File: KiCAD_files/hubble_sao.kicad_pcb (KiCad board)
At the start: 2 copper layers, 38 x 45.5 mm, 43 parts, among them J1 Conn_02x03_Counter_Clockwise, J2 Conn_02x03_Odd_Even, Q1 DMP3099L-7, SW1 SW_Push_Shielded, SW2 SW_Push, U1 VEML3328, U2 LSM6DSO, U3 ATmega328PB-A, U4 TLV9062xD, U5 TLV9062xD

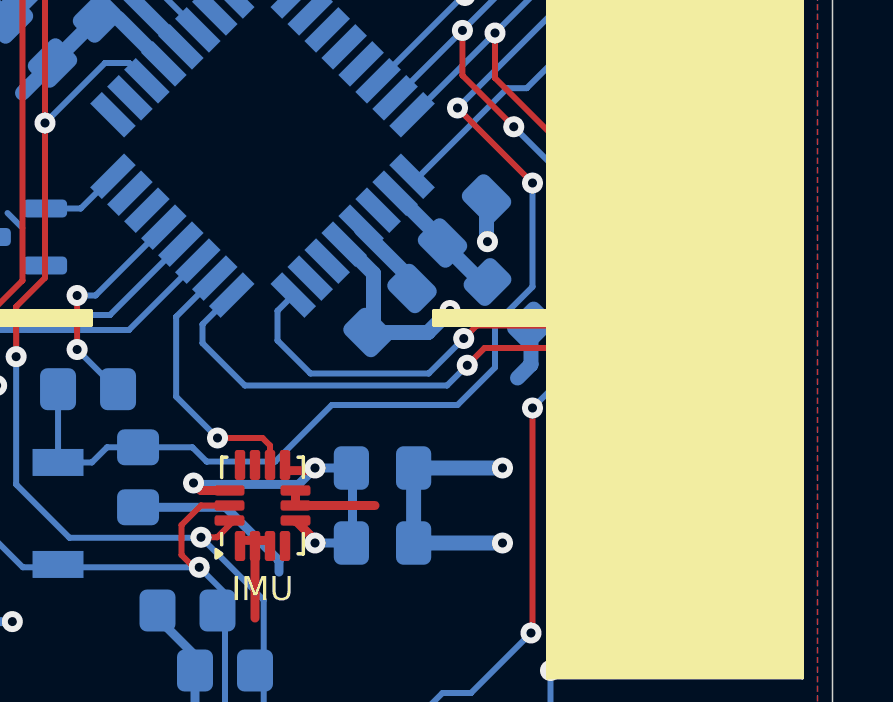
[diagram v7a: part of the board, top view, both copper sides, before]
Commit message: Moved Panel3 to 19/PE2/ADC6/ICP3
This should enable the use of the Input Capture Pin 3.
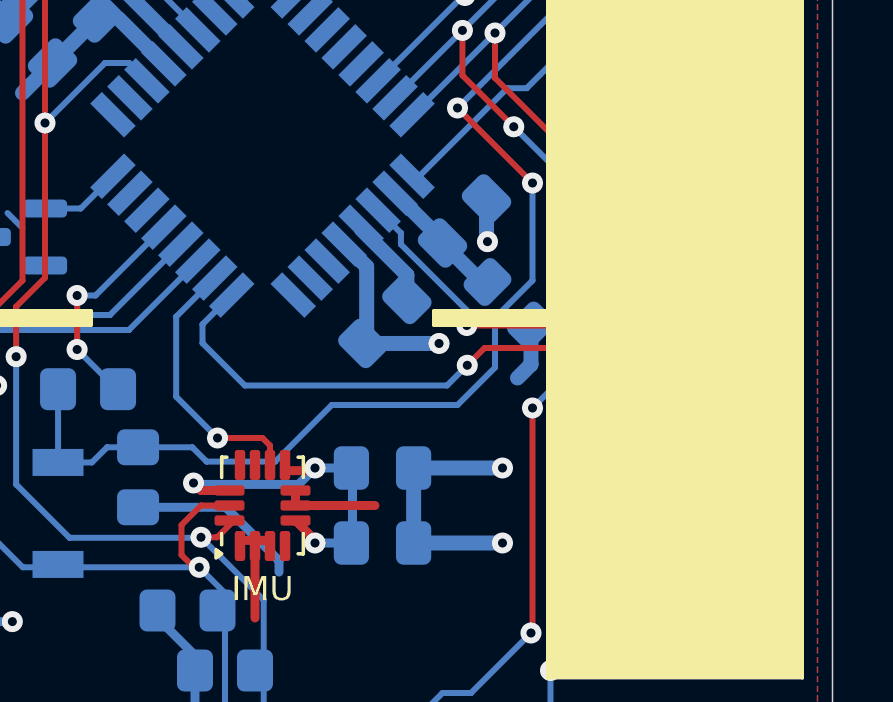
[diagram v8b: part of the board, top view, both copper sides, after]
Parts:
- moved C7 0.40 mm to (94.1, 124.6)
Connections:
- U3 pad 19: unconnected-(U3-PE2-Pad19) -> /PANEL3
- U3 pad 24: /PANEL3 -> unconnected-(U3-PC1-Pad24)
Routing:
- net /PANEL3: track 21.9 -> 17.8 mm
- net GND: track 65.9 -> 65.2 mm
- net Net-(U3-AREF): track 2.40 -> 2.98 mm
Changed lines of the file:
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@@
 	(net 10 "unconnected-(U3-XTAL1{slash}PB6-Pad7)")
 	(net 11 "unconnected-(U3-PD0-Pad30)")
-	(net 12 "unconnected-(U3-PE2-Pad19)")
+	(net 12 "unconnected-(U3-PC1-Pad24)")
 	(net 13 "unconnected-(U3-PD1-Pad31)")
 	(net 14 "/LED")
@@
 			(size 1.6 0.55)
 			(layers "B.Cu" "B.Paste" "B.Mask")
-			(net 12 "unconnected-(U3-PE2-Pad19)")
+			(net 28 "/PANEL3")
 			(pinfunction "PE2")
-			(pintype "bidirectional+no_connect")
+			(pintype "bidirectional")
 		)
 		(pad "20" smd rect
@@
 			(size 1.6 0.55)
 			(layers "B.Cu" "B.Paste" "B.Mask")
-			(net 28 "/PANEL3")
+			(net 12 "unconnected-(U3-PC1-Pad24)")
 			(pinfunction "PC1")
-			(pintype "bidirectional")
+			(pintype "bidirectional+no_connect")
 		)
 		(pad "25" smd rect
@@
 	(footprint "Capacitor_SMD:C_0805_2012Metric_Pad1.18x1.45mm_HandSolder"
 		(layer "B.Cu")
-		(at 94.25 124.25 45)
+		(at 94.078623 124.615377 45)
 		(descr "Capacitor SMD 0805 (2012 Metric), square (rectangular) end terminal, IPC_7351 nominal with elongated pad for handsoldering. (Body size source: IPC-SM-782 page 76, https://www.pcb-3d.com/wordpress/wp-content/uploads/ipc-sm-782a_amendment_1_and_2.pdf, https://docs.google.com/spreadsheets/d/1BsfQQcO9C6DZCsRaXUlFlo91Tg2WpOkGARC1WS5S8t0/edit?usp=sharing), generated with kicad-footprint-generator")
 		(tags "capacitor handsolder")
@@
 	)
 	(segment
+		(start 94.812246 123.062246)
+		(end 94.812246 123.881754)
+		(width 0.5)
+		(layer "B.Cu")
+		(net 7)
+	)
+	(segment
 		(start 93.288047 121.538047)
-		(end 94.983623 123.233623)
+		(end 94.812246 123.062246)
 		(width 0.5)
 		(layer "B.Cu")
@@
 	)
 	(via
-		(at 96.25 124.25)
+		(at 95.885 125.349)
 		(size 0.7)
 		(drill 0.3)
@@
 	)
 	(via
-		(at 100.25 130.25)
+		(at 100.457 130.175)
 		(size 0.7)
 		(drill 0.3)
@@
 	)
 	(segment
+		(start 101.4195 131.1375)
+		(end 101.5 131.1375)
+		(width 0.3)
+		(layer "B.Cu")
+		(net 20)
+	)
+	(segment
 		(start 73.5 127.11)
 		(end 74.62 127.11)
@@
 	)
 	(segment
-		(start 79.883 132.487)
-		(end 79.883 133.604)
-		(width 0.3)
+		(start 93.472 122.787686)
+		(end 92.722361 122.038047)
+		(width 0.5)
+		(layer "B.Cu")
+		(net 20)
+	)
+	(segment
+		(start 95.885 125.349)
+		(end 93.881754 125.349)
+		(width 0.5)
 		(layer "B.Cu")
 		(net 20)
 	)
 	(segment
-		(start 101.5 131.1375)
-		(end 101.1375 131.1375)
+		(start 79.883 132.487)
+		(end 79.883 133.604)
 		(width 0.3)
 		(layer "B.Cu")
@@
 	)
 	(segment
-		(start 93.7 124.8)
-		(end 93.7 123.015686)
+		(start 93.472 125.349)
+		(end 93.472 122.787686)
 		(width 0.5)
 		(layer "B.Cu")
@@
 	)
 	(segment
-		(start 101.1375 131.1375)
-		(end 100.25 130.25)
-		(width 0.3)
-		(layer "B.Cu")
-		(net 20)
-	)
-	(segment
 		(start 91.25 103)
 		(end 92.25 104)
@@
 	)
 	(segment
+		(start 100.457 130.175)
+		(end 101.4195 131.1375)
+		(width 0.3)
+		(layer "B.Cu")
+		(net 20)
+	)
+	(segment
 		(start 100.098 109.75)
 		(end 101.346 110.998)
@@
 	)
 	(segment
-		(start 83.032754 112.467246)
-		(end 83.032754 113.032754)
-		(width 0.5)
+		(start 92.722361 122.038047)
+		(end 92.849361 122.038047)
+		(width 0.3)
 		(layer "B.Cu")
 		(net 20)
 	)
 	(segment
-		(start 93.7 123.015686)
-		(end 92.722361 122.038047)
+		(start 83.032754 112.467246)
+		(end 83.032754 113.032754)
 		(width 0.5)
 		(layer "B.Cu")
@@
 	)
 	(segment
-		(start 96.25 124.25)
-		(end 95.516377 124.983623)
-		(width 0.5)
-		(layer "B.Cu")
-		(net 20)
-	)
-	(segment
 		(start 74.62 127.11)
 		(end 75.89 127.11)
@@
 	)
 	(segment
-		(start 95.516377 124.983623)
-		(end 93.516377 124.983623)
-		(width 0.5)
-		(layer "B.Cu")
-		(net 20)
-	)
-	(segment
 		(start 94.12 140)
 		(end 92.58 141.54)
@@
 	)
 	(segment
-		(start 102 124.25)
-		(end 101.5 124.75)
-		(width 0.2)
-		(layer "F.Cu")
-		(net 28)
-	)
-	(segment
-		(start 97.141177 124.75)
-		(end 96.707666 125.183511)
+		(start 101.5 124.75)
+		(end 102 124.25)
 		(width 0.2)
 		(layer "F.Cu")
@@
 	)
 	(segment
-		(start 101.5 124.75)
-		(end 97.141177 124.75)
+		(start 96.81 124.75)
+		(end 101.5 124.75)
 		(width 0.2)
 		(layer "F.Cu")
@@
 	)
 	(via
-		(at 96.707666 125.183511)
+		(at 96.81 124.75)
 		(size 0.7)
 		(drill 0.3)
@@
 	)
 	(segment
-		(start 90.5 124.260408)
-		(end 91.025305 123.735103)
-		(width 0.2)
-		(layer "B.Cu")
-		(net 28)
-	)
-	(segment
-		(start 90.5 125.25)
-		(end 90.5 124.260408)
+		(start 94.615 121.667944)
+		(end 93.853732 120.906676)
 		(width 0.2)
 		(layer "B.Cu")
@@
 	)
 	(segment
+		(start 96.81 124.242)
+		(end 94.615 122.047)
+		(width 0.2)
+		(layer "B.Cu")
+		(net 28)
+	)
+	(segment
 		(start 102 124.25)
 		(end 102.095 124.155)
@@
 	)
 	(segment
-		(start 102.7125 117.2875)
-		(end 102.75 117.25)
-		(width 0.2)
-		(layer "B.Cu")
-		(net 28)
-	)
-	(segment
-		(start 95.541177 126.35)
-		(end 91.6 126.35)
+		(start 96.81 124.75)
+		(end 96.81 124.242)
 		(width 0.2)
 		(layer "B.Cu")
@@
 	)
 	(segment
-		(start 91.6 126.35)
-		(end 90.5 125.25)
+		(start 102.7125 117.2875)
+		(end 102.75 117.25)
 		(width 0.2)
 		(layer "B.Cu")
@@
 	)
 	(segment
-		(start 96.707666 125.183511)
-		(end 95.541177 126.35)
+		(start 94.615 122.047)
+		(end 94.615 121.667944)
 		(width 0.2)
 		(layer "B.Cu")
@@
 	)
 	(segment
-		(start 87.662 128.81)
-		(end 85.852 128.81)
+		(start 97.75 124.5)
+		(end 97.75 126.151)
 		(width 0.2)
 		(layer "B.Cu")
@@
 	)
 	(segment
-		(start 99 123.46213)
-		(end 97.75 124.71213)
+		(start 97.75 126.151)
+		(end 96.501 127.4)
 		(width 0.2)
 		(layer "B.Cu")
@@
 	)
 	(segment
-		(start 88.138 129.286)
-		(end 87.662 128.81)
+		(start 96.501 127.4)
+		(end 92.31 127.4)
 		(width 0.2)
 		(layer "B.Cu")
@@
 	)
 	(segment
-		(start 96.501 127.4)
-		(end 92.31 127.4)
+		(start 87.662 128.81)
+		(end 85.852 128.81)
 		(width 0.2)
 		(layer "B.Cu")
@@
 	)
 	(segment
-		(start 84.818499 128.81)
-		(end 84.313501 129.314998)
+		(start 88.138 129.286)
+		(end 87.662 128.81)
 		(width 0.2)
 		(layer "B.Cu")
@@
 	)
 	(segment
-		(start 96.5 117.5)
-		(end 100.3604 113.6396)
+		(start 99 123.25)
+		(end 97.75 124.5)
 		(width 0.2)
 		(layer "B.Cu")
@@
 	)
 	(segment
-		(start 83.185 129.314998)
-		(end 83.185 126.873)
+		(start 84.818499 128.81)
+		(end 84.313501 129.314998)
 		(width 0.2)
 		(layer "B.Cu")
@@
 	)
 	(segment
-		(start 100.3604 113.6396)
-		(end 101.346 113.6396)
+		(start 96.5 117.5)
+		(end 100.3604 113.6396)
 		(width 0.2)
 		(layer "B.Cu")
@@
 	)
 	(segment
-		(start 97.75 124.71213)
-		(end 97.75 126.151)
+		(start 83.185 129.314998)
+		(end 83.185 126.873)
 		(width 0.2)
 		(layer "B.Cu")
@@
 	)
 	(segment
-		(start 97.75 126.151)
-		(end 96.501 127.4)
+		(start 100.3604 113.6396)
+		(end 101.346 113.6396)
 		(width 0.2)
 		(layer "B.Cu")
@@
 	)
 	(segment
-		(start 85.852 128.81)
-		(end 84.818499 128.81)
+		(start 90.424 129.286)
+		(end 88.138 129.286)
 		(width 0.2)
 		(layer "B.Cu")
@@
 	)
 	(segment
-		(start 99 120)
-		(end 99 123.46213)
+		(start 85.852 128.81)
+		(end 84.818499 128.81)
 		(width 0.2)
 		(layer "B.Cu")
@@
 	)
 	(segment
-		(start 90.424 129.286)
-		(end 88.138 129.286)
+		(start 99 120)
+		(end 99 123.25)
 		(width 0.2)
 		(layer "B.Cu")
